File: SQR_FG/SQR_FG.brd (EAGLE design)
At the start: 100 x 80 mm, 15 parts, among them IC1 MEGA328P, IC2 NJM7032, Q1 16MHz, SW1 EC12E_SW

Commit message: SQR_FG MOS-FET Switch
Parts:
- removed R9: (no value), rcl:0207/7
- added C3, C4, C5: 0.1uF, rcl:C025-024X044
- added R3: 33k, rcl:0207/7
- added T1, T2: (no value), zetex:E3LINE
- JP2: value Output -> (none); device pinhead:1X03 -> pinhead:1X02
- R6: value (none) -> 10
- R7, R8: value (none) -> 10k
- moved JP2 61.4 mm to (-101.6, -157.5)
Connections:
- removed net N$14: IC2.6, IC2.7, R9.1
- new net N$12: IC1.17, T2.2
- new net N$13: IC1.18, T1.2
- new net N$6: JP2.2, R10.1, T1.1, T2.1
- new net N$8: R10.3, R3.1
- net +5V: now also C3.1, C4.2, C5.1, IC1.20
- net GND: now also C3.2, C4.1, C5.2, T2.3; no longer IC1.20, JP2.3, R10.1
- net VGND: now also IC2.6, IC2.7, T1.3; no longer JP2.2, R9.2
- net WAVE_OUT: now also R3.2; no longer R10.3
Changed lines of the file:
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@@
 <setting verticaltext="up"/>
 </settings>
-<grid distance="0.05" unitdist="inch" unit="inch" style="lines" multiple="1" display="no" altdistance="0.025" altunitdist="inch" altunit="inch"/>
+<grid distance="0.1" unitdist="inch" unit="inch" style="dots" multiple="1" display="yes" altdistance="0.05" altunitdist="inch" altunit="inch"/>
 <layers>
 <layer number="1" name="Top" color="4" fill="1" visible="yes" active="yes"/>
@@
 </element>
 <element name="IC2" library="linear" package="DIL08" value="NJM7032" x="-80.01" y="-85.09"/>
-<element name="R6" library="rcl" package="0207/7" value="" x="-82.55" y="-93.98"/>
-<element name="JP2" library="pinhead" package="1X03" value="Output" x="-82.55" y="-99.06"/>
-<element name="R7" library="rcl" package="0207/7" value="" x="-82.55" y="-106.68"/>
-<element name="R8" library="rcl" package="0207/7" value="" x="-82.55" y="-111.76"/>
-<element name="R9" library="rcl" package="0207/7" value="" x="-82.55" y="-116.84"/>
+<element name="R6" library="rcl" package="0207/7" value="10" x="-82.55" y="-93.98"/>
+<element name="R7" library="rcl" package="0207/7" value="10k" x="-82.55" y="-106.68"/>
+<element name="R8" library="rcl" package="0207/7" value="10k" x="-82.55" y="-111.76"/>
 <element name="R10" library="pot" package="3RP/1610N" value="10k" x="-96.52" y="-104.14"/>
+<element name="C3" library="rcl" package="C025-024X044" value="0.1uF" x="-102.87" y="-121.92"/>
+<element name="C4" library="rcl" package="C025-024X044" value="0.1uF" x="-102.87" y="-127"/>
+<element name="T1" library="zetex" package="E3LINE" value="" x="-102.87" y="-134.62">
+<attribute name="OC_NEWARK" value="unknown" x="-102.87" y="-134.62" size="1.778" layer="27" display="off"/>
+<attribute name="MPN" value="" x="-102.87" y="-134.62" size="1.778" layer="27" display="off"/>
+<attribute name="MF" value="" x="-102.87" y="-134.62" size="1.778" layer="27" display="off"/>
+<attribute name="OC_FARNELL" value="unknown" x="-102.87" y="-134.62" size="1.778" layer="27" display="off"/>
+</element>
+<element name="T2" library="zetex" package="E3LINE" value="" x="-102.87" y="-142.24">
+<attribute name="OC_NEWARK" value="unknown" x="-102.87" y="-142.24" size="1.778" layer="27" display="off"/>
+<attribute name="MPN" value="" x="-102.87" y="-142.24" size="1.778" layer="27" display="off"/>
+<attribute name="MF" value="" x="-102.87" y="-142.24" size="1.778" layer="27" display="off"/>
+<attribute name="OC_FARNELL" value="unknown" x="-102.87" y="-142.24" size="1.778" layer="27" display="off"/>
+</element>
+<element name="C5" library="rcl" package="C025-024X044" value="0.1uF" x="-101.6" y="-149.86"/>
+<element name="JP2" library="pinhead" package="1X02" value="" x="-101.6" y="-157.48"/>
+<element name="R3" library="rcl" package="0207/7" value="33k" x="-99.06" y="-165.1"/>
 </elements>
 <signals>
@@
 <contactref element="C2" pad="1"/>
 <contactref element="IC1" pad="22"/>
-<contactref element="IC1" pad="20"/>
 <contactref element="JP1" pad="4"/>
 <contactref element="R2" pad="3"/>
@@
 <contactref element="SW1" pad="D"/>
 <contactref element="IC2" pad="4"/>
-<contactref element="JP2" pad="3"/>
 <contactref element="R8" pad="1"/>
-<contactref element="R10" pad="1"/>
-<wire x1="-86.36" y1="-111.76" x2="-101.52" y2="-104.14" width="0" layer="19" extent="1-1"/>
-<wire x1="-80.01" y1="-99.06" x2="-86.36" y2="-111.76" width="0" layer="19" extent="1-1"/>
-<wire x1="-76.2" y1="-88.9" x2="-80.01" y2="-99.06" width="0" layer="19" extent="1-1"/>
+<contactref element="C4" pad="1"/>
+<contactref element="C3" pad="2"/>
+<contactref element="T2" pad="3"/>
+<contactref element="C5" pad="2"/>
+<wire x1="-102.87" y1="-140.97" x2="-100.33" y2="-149.86" width="0" layer="19" extent="1-1"/>
+<wire x1="-104.14" y1="-127" x2="-102.87" y2="-140.97" width="0" layer="19" extent="1-1"/>
+<wire x1="-101.6" y1="-121.92" x2="-104.14" y2="-127" width="0" layer="19" extent="1-1"/>
+<wire x1="-86.36" y1="-111.76" x2="-101.6" y2="-121.92" width="0" layer="19" extent="1-1"/>
+<wire x1="-76.2" y1="-88.9" x2="-86.36" y2="-111.76" width="0" layer="19" extent="1-1"/>
 <wire x1="-80.01" y1="-27.82" x2="-76.2" y2="-88.9" width="0" layer="19" extent="1-1"/>
 <wire x1="-82.51" y1="-13.32" x2="-80.01" y2="-27.82" width="0" layer="19" extent="1-1"/>
@@
 <wire x1="-30.48" y1="2.54" x2="-52.07" y2="-12.7" width="0" layer="19" extent="1-1"/>
 <wire x1="-33.02" y1="10.16" x2="-30.48" y2="2.54" width="0" layer="19" extent="1-1"/>
-<wire x1="-27.94" y1="10.16" x2="-33.02" y2="10.16" width="0" layer="19" extent="1-1"/>
 </signal>
 <signal name="N$1">
@@
 <contactref element="IC1" pad="7"/>
 <contactref element="R2" pad="1"/>
+<contactref element="R7" pad="2"/>
+<contactref element="IC1" pad="20"/>
+<contactref element="C3" pad="1"/>
+<contactref element="C4" pad="2"/>
 <contactref element="IC2" pad="8"/>
-<contactref element="R7" pad="2"/>
+<contactref element="C5" pad="1"/>
+<wire x1="-101.6" y1="-127" x2="-102.87" y2="-149.86" width="0" layer="19" extent="1-1"/>
+<wire x1="-104.14" y1="-121.92" x2="-101.6" y2="-127" width="0" layer="19" extent="1-1"/>
+<wire x1="-78.74" y1="-106.68" x2="-104.14" y2="-121.92" width="0" layer="19" extent="1-1"/>
 <wire x1="-83.82" y1="-81.28" x2="-78.74" y2="-106.68" width="0" layer="19" extent="1-1"/>
 <wire x1="-67.23" y1="-17.78" x2="-83.82" y2="-81.28" width="0" layer="19" extent="1-1"/>
 <wire x1="-52.07" y1="-22.86" x2="-67.23" y2="-17.78" width="0" layer="19" extent="1-1"/>
 <wire x1="-33.02" y1="2.54" x2="-52.07" y2="-22.86" width="0" layer="19" extent="1-1"/>
+<wire x1="-27.94" y1="10.16" x2="-33.02" y2="2.54" width="0" layer="19" extent="1-1"/>
 </signal>
 <signal name="SDA">
@@
 <signal name="WAVE_OUT">
 <contactref element="IC1" pad="16"/>
-<contactref element="R10" pad="3"/>
-<wire x1="-17.78" y1="10.16" x2="-91.52" y2="-104.14" width="0" layer="19" extent="1-1"/>
+<contactref element="R3" pad="2"/>
+<wire x1="-95.25" y1="-165.1" x2="-17.78" y2="10.16" width="0" layer="19" extent="1-1"/>
 </signal>
 <signal name="N$5">
@@
 <contactref element="R6" pad="2"/>
 <contactref element="JP2" pad="1"/>
-<wire x1="-78.74" y1="-93.98" x2="-85.09" y2="-99.06" width="0" layer="19" extent="1-1"/>
-</signal>
-<signal name="N$14">
-<contactref element="IC2" pad="6"/>
-<contactref element="IC2" pad="7"/>
-<contactref element="R9" pad="1"/>
-<wire x1="-81.28" y1="-81.28" x2="-86.36" y2="-116.84" width="0" layer="19" extent="1-1"/>
-<wire x1="-78.74" y1="-81.28" x2="-81.28" y2="-81.28" width="0" layer="19" extent="1-1"/>
+<wire x1="-102.87" y1="-157.48" x2="-78.74" y2="-93.98" width="0" layer="19" extent="1-1"/>
 </signal>
 <signal name="N$17">
@@
 <wire x1="-76.2" y1="-81.28" x2="-86.36" y2="-106.68" width="0" layer="19" extent="1-1"/>
 </signal>
-<signal name="VGND">
-<contactref element="JP2" pad="2"/>
-<contactref element="R9" pad="2"/>
-<wire x1="-82.55" y1="-99.06" x2="-78.74" y2="-116.84" width="0" layer="19" extent="1-1"/>
-</signal>
 <signal name="N$4">
 <contactref element="R10" pad="2"/>
@@
 <wire x1="-78.74" y1="-88.9" x2="-96.52" y2="-104.14" width="0" layer="19" extent="1-1"/>
 </signal>
+<signal name="N$6">
+<contactref element="R10" pad="1"/>
+<contactref element="T1" pad="1"/>
+<contactref element="T2" pad="1"/>
+<contactref element="JP2" pad="2"/>
+<wire x1="-102.87" y1="-135.89" x2="-102.87" y2="-143.51" width="0" layer="19" extent="1-1"/>
+<wire x1="-100.33" y1="-157.48" x2="-102.87" y2="-143.51" width="0" layer="19" extent="1-1"/>
+<wire x1="-101.52" y1="-104.14" x2="-102.87" y2="-135.89" width="0" layer="19" extent="1-1"/>
+</signal>
+<signal name="N$12">
+<contactref element="IC1" pad="17"/>
+<contactref element="T2" pad="2"/>
+<wire x1="-20.32" y1="10.16" x2="-102.87" y2="-142.24" width="0" layer="19" extent="1-1"/>
+</signal>
+<signal name="N$13">
+<contactref element="IC1" pad="18"/>
+<contactref element="T1" pad="2"/>
+<wire x1="-22.86" y1="10.16" x2="-102.87" y2="-134.62" width="0" layer="19" extent="1-1"/>
+</signal>
+<signal name="VGND">
+<contactref element="IC2" pad="7"/>
+<contactref element="IC2" pad="6"/>
+<contactref element="T1" pad="3"/>
+<wire x1="-81.28" y1="-81.28" x2="-102.87" y2="-133.35" width="0" layer="19" extent="1-1"/>
+<wire x1="-78.74" y1="-81.28" x2="-81.28" y2="-81.28" width="0" layer="19" extent="1-1"/>
+</signal>
+<signal name="N$8">
+<contactref element="R10" pad="3"/>
+<contactref element="R3" pad="1"/>
+<wire x1="-102.87" y1="-165.1" x2="-91.52" y2="-104.14" width="0" layer="19" extent="1-1"/>
+</signal>
 </signals>

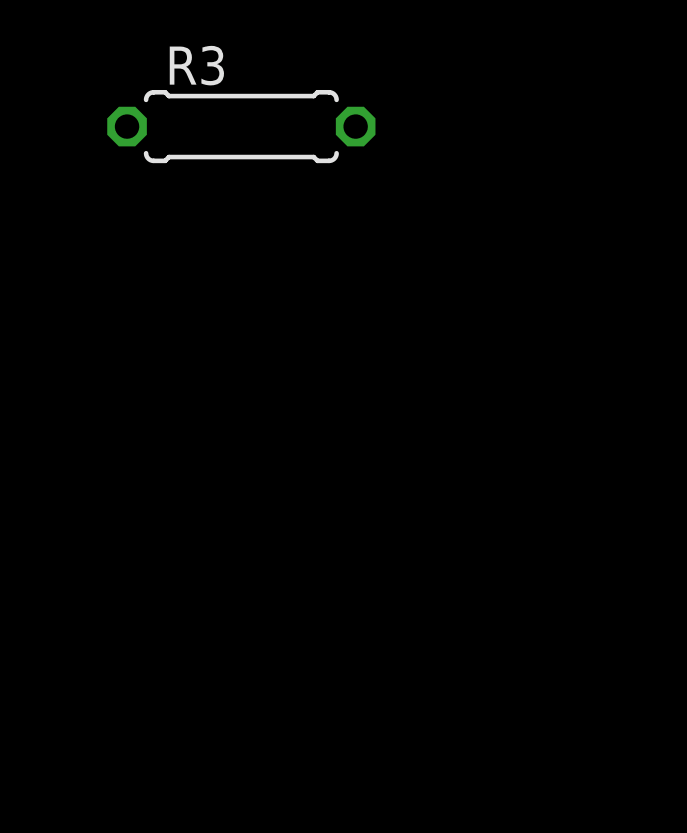
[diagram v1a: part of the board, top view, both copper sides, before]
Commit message: SQR_FG Add 2nd VCVS LPF
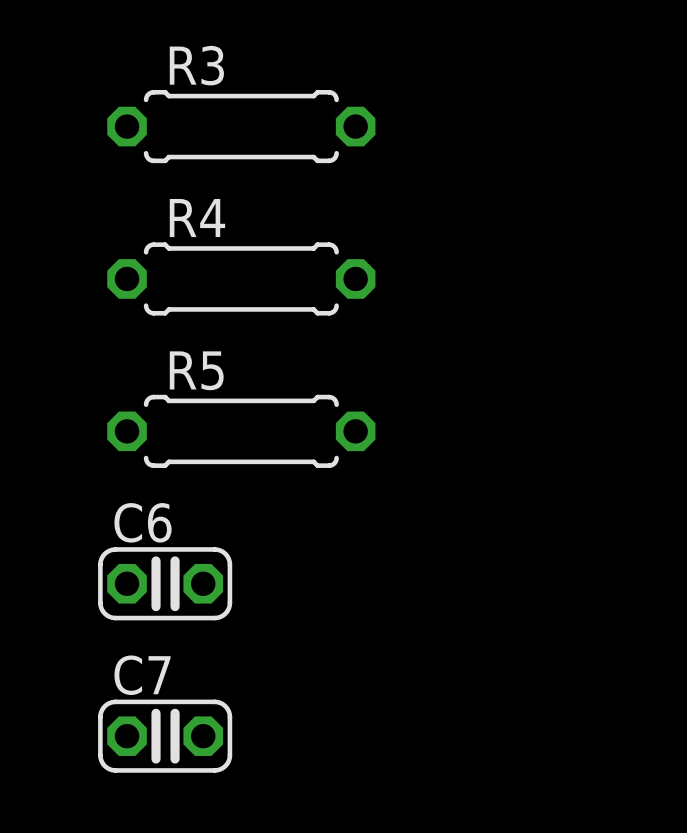
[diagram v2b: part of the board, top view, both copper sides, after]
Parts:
- added C6, C7: (no value), rcl:C025-024X044
- added R4, R5: (no value), rcl:0207/7
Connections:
- new net N$14: C6.2, IC2.3, R4.2
- new net N$15: R5.1
- net GND: now also C6.1
- net N$16: now also C7.2
- net N$4: now also C7.1, R4.1, R5.2; no longer IC2.3, R10.2
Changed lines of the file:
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@@
 <element name="JP2" library="pinhead" package="1X02" value="" x="-101.6" y="-157.48"/>
 <element name="R3" library="rcl" package="0207/7" value="33k" x="-99.06" y="-165.1"/>
+<element name="R4" library="rcl" package="0207/7" value="" x="-99.06" y="-170.18"/>
+<element name="R5" library="rcl" package="0207/7" value="" x="-99.06" y="-175.26"/>
+<element name="C6" library="rcl" package="C025-024X044" value="" x="-101.6" y="-180.34"/>
+<element name="C7" library="rcl" package="C025-024X044" value="" x="-101.6" y="-185.42"/>
 </elements>
 <signals>
@@
 <contactref element="T2" pad="3"/>
 <contactref element="C5" pad="2"/>
+<contactref element="C6" pad="1"/>
 <wire x1="-102.87" y1="-140.97" x2="-100.33" y2="-149.86" width="0" layer="19" extent="1-1"/>
 <wire x1="-104.14" y1="-127" x2="-102.87" y2="-140.97" width="0" layer="19" extent="1-1"/>
@@
 <wire x1="-86.36" y1="-111.76" x2="-101.6" y2="-121.92" width="0" layer="19" extent="1-1"/>
 <wire x1="-76.2" y1="-88.9" x2="-86.36" y2="-111.76" width="0" layer="19" extent="1-1"/>
+<wire x1="-102.87" y1="-180.34" x2="-100.33" y2="-149.86" width="0" layer="19" extent="1-1"/>
 <wire x1="-80.01" y1="-27.82" x2="-76.2" y2="-88.9" width="0" layer="19" extent="1-1"/>
 <wire x1="-82.51" y1="-13.32" x2="-80.01" y2="-27.82" width="0" layer="19" extent="1-1"/>
@@
 <contactref element="IC2" pad="1"/>
 <contactref element="R6" pad="1"/>
+<contactref element="C7" pad="2"/>
 <wire x1="-83.82" y1="-88.9" x2="-86.36" y2="-93.98" width="0" layer="19" extent="1-1"/>
 <wire x1="-81.28" y1="-88.9" x2="-83.82" y2="-88.9" width="0" layer="19" extent="1-1"/>
+<wire x1="-100.33" y1="-185.42" x2="-86.36" y2="-93.98" width="0" layer="19" extent="1-1"/>
 </signal>
 <signal name="N$11">
@@
 <wire x1="-78.74" y1="-111.76" x2="-86.36" y2="-106.68" width="0" layer="19" extent="1-1"/>
 <wire x1="-76.2" y1="-81.28" x2="-86.36" y2="-106.68" width="0" layer="19" extent="1-1"/>
-</signal>
-<signal name="N$4">
-<contactref element="R10" pad="2"/>
-<contactref element="IC2" pad="3"/>
-<wire x1="-78.74" y1="-88.9" x2="-96.52" y2="-104.14" width="0" layer="19" extent="1-1"/>
 </signal>
 <signal name="N$6">
@@
 <wire x1="-102.87" y1="-165.1" x2="-91.52" y2="-104.14" width="0" layer="19" extent="1-1"/>
 </signal>
+<signal name="N$4">
+<contactref element="R5" pad="2"/>
+<contactref element="R4" pad="1"/>
+<contactref element="C7" pad="1"/>
+<wire x1="-95.25" y1="-175.26" x2="-102.87" y2="-185.42" width="0" layer="19" extent="1-1"/>
+<wire x1="-102.87" y1="-170.18" x2="-95.25" y2="-175.26" width="0" layer="19" extent="1-1"/>
+</signal>
+<signal name="N$14">
+<contactref element="R4" pad="2"/>
+<contactref element="IC2" pad="3"/>
+<contactref element="C6" pad="2"/>
+<wire x1="-95.25" y1="-170.18" x2="-78.74" y2="-88.9" width="0" layer="19" extent="1-1"/>
+<wire x1="-100.33" y1="-180.34" x2="-95.25" y2="-170.18" width="0" layer="19" extent="1-1"/>
+</signal>
+<signal name="N$15">
+<contactref element="R5" pad="1"/>
+</signal>
 </signals>

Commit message: SQR_FG Bypass by C
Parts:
- removed C7: (no value), rcl:C025-024X044
- removed R4, R5: (no value), rcl:0207/7
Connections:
- removed net N$14: C6.2, IC2.3, R4.2
- removed net N$4: C7.1, R4.1, R5.2
- net N$15: now also C6.2, IC2.3; no longer R5.1
- net N$16: no longer C7.2
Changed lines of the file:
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@@
 <element name="JP2" library="pinhead" package="1X02" value="" x="-101.6" y="-157.48"/>
 <element name="R3" library="rcl" package="0207/7" value="33k" x="-99.06" y="-165.1"/>
-<element name="R4" library="rcl" package="0207/7" value="" x="-99.06" y="-170.18"/>
-<element name="R5" library="rcl" package="0207/7" value="" x="-99.06" y="-175.26"/>
 <element name="C6" library="rcl" package="C025-024X044" value="" x="-101.6" y="-180.34"/>
-<element name="C7" library="rcl" package="C025-024X044" value="" x="-101.6" y="-185.42"/>
 </elements>
 <signals>
@@
 <contactref element="IC2" pad="1"/>
 <contactref element="R6" pad="1"/>
-<contactref element="C7" pad="2"/>
 <wire x1="-83.82" y1="-88.9" x2="-86.36" y2="-93.98" width="0" layer="19" extent="1-1"/>
 <wire x1="-81.28" y1="-88.9" x2="-83.82" y2="-88.9" width="0" layer="19" extent="1-1"/>
-<wire x1="-100.33" y1="-185.42" x2="-86.36" y2="-93.98" width="0" layer="19" extent="1-1"/>
 </signal>
 <signal name="N$11">
@@
 <wire x1="-102.87" y1="-165.1" x2="-91.52" y2="-104.14" width="0" layer="19" extent="1-1"/>
 </signal>
-<signal name="N$4">
-<contactref element="R5" pad="2"/>
-<contactref element="R4" pad="1"/>
-<contactref element="C7" pad="1"/>
-<wire x1="-95.25" y1="-175.26" x2="-102.87" y2="-185.42" width="0" layer="19" extent="1-1"/>
-<wire x1="-102.87" y1="-170.18" x2="-95.25" y2="-175.26" width="0" layer="19" extent="1-1"/>
-</signal>
-<signal name="N$14">
-<contactref element="R4" pad="2"/>
+<signal name="N$15">
+<contactref element="C6" pad="2"/>
 <contactref element="IC2" pad="3"/>
-<contactref element="C6" pad="2"/>
-<wire x1="-95.25" y1="-170.18" x2="-78.74" y2="-88.9" width="0" layer="19" extent="1-1"/>
-<wire x1="-100.33" y1="-180.34" x2="-95.25" y2="-170.18" width="0" layer="19" extent="1-1"/>
-</signal>
-<signal name="N$15">
-<contactref element="R5" pad="1"/>
+<wire x1="-100.33" y1="-180.34" x2="-78.74" y2="-88.9" width="0" layer="19" extent="1-1"/>
 </signal>
 </signals>

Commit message: SQR_FG.sch changed
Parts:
- added C7: (no value), rcl:E2,5-5
- added R4: 22k, rcl:0207/7
- added R5: 12k, rcl:0207/7
- C3: value 0.1uF -> (none); device rcl:C025-024X044 -> rcl:E2,5-5
- JP2: value (none) -> OUT
- moved C6 244.6 mm to (53.3, 8.89), turned to 90 degrees
- moved JP2 236.0 mm to (30.5, 38.1), turned to 180 degrees
- moved C5 221.5 mm to (43.2, 17.8)
- moved T2 211.4 mm to (29.2, 22.9)
- moved R3 208.5 mm to (17.8, 7.62), turned to 180 degrees
- moved T1 204.9 mm to (36.8, 15.2)
- moved R10 200.1 mm to (71.1, 5.08), turned to 90 degrees
- moved R7 190.4 mm to (54.6, 25.4)
- moved R8 186.9 mm to (44.5, 25.4)
- moved C4 186.3 mm to (2.54, 26.7), turned to 270 degrees
- moved SW1 172.2 mm to (80.0, 43.2)
- moved IC2 166.6 mm to (52.1, 16.5)
- moved R6 164.9 mm to (48.3, 6.35), turned to 90 degrees
- moved R2 148.6 mm to (80.0, 25.4)
- moved JP1 112.5 mm to (61.0, 20.3), turned to 90 degrees
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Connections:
- net N$10 renamed RE_SW
- net N$12 renamed SW_GND
- net N$13 renamed SW_VGND
- net N$5 renamed RE_A
- net N$7 renamed RE_B
- new net AGND: C5.2, C6.1, C7.-, IC2.4, R8.1, T2.3
- new net N$4: IC1.13, R4.1
- net +5V: now also C3.+; no longer C3.1
- net GND: now also R5.2; no longer C3.2, C5.2, C6.1, IC2.4, R8.1, T2.3
- net N$17: now also C3.-, C7.+
- net RST: now also R4.2, R5.1; no longer IC1.13
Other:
- board size 100 x 80 mm -> 96.2 x 58.4 mm

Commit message: SQR_FG Schematic Updated
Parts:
- C3, C7: value (none) -> 100uF
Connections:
- removed net N$4: IC1.13, R4.1
- new net LCD_RST: IC1.26, R4.1
- net RE_A: now also IC1.2; no longer IC1.4
- net RE_B: now also IC1.3; no longer IC1.5
- net RE_SW: now also IC1.4; no longer IC1.6
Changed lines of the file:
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@@
 <element name="R4" library="rcl" package="0207/7" value="22k" x="-45.72" y="-33.02"/>
 <element name="R5" library="rcl" package="0207/7" value="12k" x="-45.72" y="-38.1"/>
-<element name="C3" library="rcl" package="E2,5-5" value="" x="-45.72" y="-43.18"/>
-<element name="C7" library="rcl" package="E2,5-5" value="" x="-45.72" y="-50.8"/>
+<element name="C3" library="rcl" package="E2,5-5" value="100uF" x="-45.72" y="-43.18"/>
+<element name="C7" library="rcl" package="E2,5-5" value="100uF" x="-45.72" y="-50.8"/>
 </elements>
 <signals>
@@
 <wire x1="12.7" y1="7.62" x2="13.97" y2="7.62" width="0" layer="19" extent="1-1"/>
 </signal>
-<signal name="RE_A">
-<contactref element="IC1" pad="4"/>
-<contactref element="SW1" pad="B"/>
-<wire x1="5.08" y1="30.48" x2="82.51" y2="35.68" width="0" layer="19" extent="1-1"/>
-</signal>
 <signal name="RE_B">
-<contactref element="IC1" pad="5"/>
 <contactref element="SW1" pad="A"/>
-<wire x1="5.08" y1="27.94" x2="77.51" y2="35.68" width="0" layer="19" extent="1-1"/>
+<contactref element="IC1" pad="3"/>
+<wire x1="5.08" y1="33.02" x2="77.51" y2="35.68" width="0" layer="19" extent="1-1"/>
 </signal>
 <signal name="RE_SW">
-<contactref element="IC1" pad="6"/>
 <contactref element="SW1" pad="E"/>
-<wire x1="5.08" y1="25.4" x2="82.51" y2="50.18" width="0" layer="19" extent="1-1"/>
+<contactref element="IC1" pad="4"/>
+<wire x1="5.08" y1="30.48" x2="82.51" y2="50.18" width="0" layer="19" extent="1-1"/>
 </signal>
 <signal name="N$16">
@@
 <wire x1="53.34" y1="7.62" x2="55.88" y2="12.7" width="0" layer="19" extent="1-1"/>
 </signal>
-<signal name="N$4">
-<contactref element="R4" pad="1"/>
-<contactref element="IC1" pad="13"/>
-<wire x1="5.08" y1="7.62" x2="-49.53" y2="-33.02" width="0" layer="19" extent="1-1"/>
-</signal>
 <signal name="N$8">
 <contactref element="R10" pad="3"/>
@@
 <wire x1="21.59" y1="7.62" x2="71.12" y2="10.08" width="0" layer="19" extent="1-1"/>
 </signal>
+<signal name="RE_A">
+<contactref element="SW1" pad="B"/>
+<contactref element="IC1" pad="2"/>
+<wire x1="5.08" y1="35.56" x2="82.51" y2="35.68" width="0" layer="19" extent="1-1"/>
+</signal>
+<signal name="LCD_RST">
+<contactref element="IC1" pad="26"/>
+<contactref element="R4" pad="1"/>
+<wire x1="12.7" y1="33.02" x2="-49.53" y2="-33.02" width="0" layer="19" extent="1-1"/>
+</signal>
 </signals>

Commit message: Update SQR_FG.sch, SQR_FG.brd
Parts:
- removed R10: 10k, pot:3RP/1610N
- removed R2: 10k/B, pot:3RP/1610N
- removed SW1: EC12E_SW, switch-alps:ALPS_EC12E_SW
- added C10, C11, C14: 47uF, rcl:TT2D5L
- added C12, C13, C8, C9: 0.1uF, rcl:C025-024X044
- added D1: 1N4007, diode:DO41-10
- added IC3: 7805T, linear:TO220H
- added IC4: TLV1117-33, ic-package:DIL10
- added JP3: Duty, pinhead:1X03
- added JP4: Encoder, pinhead:1X04
- added JP5: Level, pinhead:1X03
- added JP6: 9V, pinhead:1X02
- C6: value (none) -> 22pF
- R3: value 33k -> 10k
- T1, T2: value (none) -> 2SK4017
- moved C3 96.1 mm to (21.6, 25.4)
- moved C7 96.1 mm to (21.6, 17.8)
- moved R5 94.3 mm to (19.1, 30.5), turned to 180 degrees
- moved R4 92.5 mm to (19.1, 33.0)
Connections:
- net +3V3: now also C13.1, IC4.5
- net +5V: now also C10.+, C11.+, C12.1, C14.+, C8.1, C9.1, IC3.1, IC3.3, IC4.3, JP3.1, JP6.1; no longer R2.1
- net GND: now also C10.-, C11.-, C12.2, C13.2, C14.-, C8.2, C9.2, IC3.2, IC4.1, JP3.3, JP4.4, JP6.2; no longer R2.3, SW1.C, SW1.D
- net N$15: now also JP5.2
- net N$6: now also JP5.3; no longer R10.1
- net N$8: now also JP5.1; no longer R10.3
- net N$9: now also JP3.2; no longer R2.2
- net RE_A: now also JP4.1; no longer SW1.B
- net RE_B: now also JP4.2; no longer SW1.A
- net RE_SW: now also JP4.3; no longer SW1.E
